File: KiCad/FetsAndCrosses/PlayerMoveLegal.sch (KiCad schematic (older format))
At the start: 0 parts

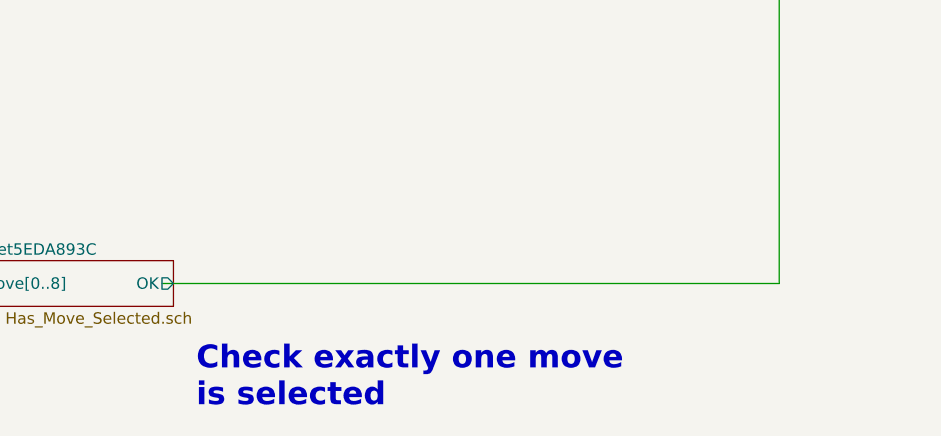
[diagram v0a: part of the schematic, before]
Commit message: Schematic Done, Footprints assigned, ERC OK.
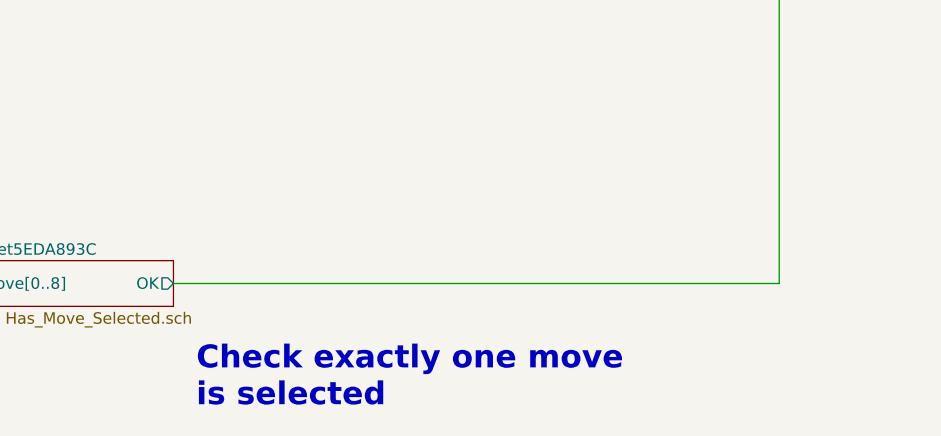
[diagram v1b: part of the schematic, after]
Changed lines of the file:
@@
 $Descr A4 11693 8268
 encoding utf-8
-Sheet 234 205
+Sheet 193 389
 Title ""
 Date ""
@@
 F4 "Move[0..8]" I L 4350 850 50
 $EndSheet
-Text Notes 5350 1500 0    100  ~ 20
-Check Selected Move \ndoes not collide with P1
-Text Notes 5350 3850 0    100  ~ 20
-Check Selected Move \ndoes not collide with P2
-Text Notes 5350 5800 0    100  ~ 20
-Check exactly one move\nis selected
 $Sheet
 S 8500 650  550  400
@@
 F5 "Q" O R 9050 850 50
 $EndSheet
+$Sheet
+S 4350 5150 900  200
+U 5EDA893D
+F0 "Sheet5EDA893C" 50
+F1 "Has_Move_Selected.sch" 50
+F2 "OK" O R 5250 5250 50
+F3 "Move[0..8]" I L 4350 5250 50
+$EndSheet
+Text Notes 5350 1500 0    100  ~ 20
+Check Selected Move \ndoes not collide with P1
+Text Notes 5350 3850 0    100  ~ 20
+Check Selected Move \ndoes not collide with P2
+Text Notes 5350 5800 0    100  ~ 20
+Check exactly one move\nis selected
 Text Notes 8700 900  0    100  ~ 20
 &
+Text HLabel 9450 850  2    50   Output ~ 0
+OK
+Text HLabel 1950 750  0    50   Input ~ 0
+Board_P1_[0..8]
+Text HLabel 2100 3000 0    50   Input ~ 0
+Board_P2_[0..8]
+Text HLabel 3700 5250 0    50   Input ~ 0
+Move[0..8]
+Text Label 3200 750  2    50   ~ 0
+Board_P1_[0..8]
+Text Label 3250 3000 2    50   ~ 0
+Board_P2_[0..8]
+Text Label 3500 750  0    50   ~ 0
+Board[0..8]
+Text Label 3550 3000 0    50   ~ 0
+Board[0..8]
 Wire Wire Line
 	5200 750  8500 750
@@
 	7800 3000 5200 3000
 Wire Wire Line
-	5200 5250 7900 5250
-Wire Wire Line
 	7900 5250 7900 950
 Wire Wire Line
@@
 Wire Wire Line
 	9050 850  9450 850
-Text HLabel 9450 850  2    50   Output ~ 0
-OK
-Text HLabel 1950 750  0    50   Input ~ 0
-Board_P1_[0..8]
-Text HLabel 2100 3000 0    50   Input ~ 0
-Board_P2_[0..8]
-Text HLabel 3700 5250 0    50   Input ~ 0
-Move[0..8]
-$Sheet
-S 4350 5150 900  200
-U 5EDA893D
-F0 "Sheet5EDA893C" 50
-F1 "Has_Move_Selected.sch" 50
-F2 "OK" O R 5250 5250 50
-F3 "Move[0..8]" I L 4350 5250 50
-$EndSheet
 Wire Bus Line
 	3700 5250 4150 5250
@@
 Wire Bus Line
 	4150 850  4350 850
-Connection ~ 4150 5250
 Wire Bus Line
 	4150 5250 4350 5250
 Wire Bus Line
 	4350 3100 4150 3100
-Connection ~ 4150 3100
 Wire Bus Line
 	4150 3100 4150 850
-Text Label 3200 750  2    50   ~ 0
-Board_P1_[0..8]
-Text Label 3250 3000 2    50   ~ 0
-Board_P2_[0..8]
-Text Label 3500 750  0    50   ~ 0
-Board[0..8]
-Text Label 3550 3000 0    50   ~ 0
-Board[0..8]
 Wire Bus Line
 	2100 3000 4350 3000
 Wire Bus Line
 	1950 750  4350 750
+Wire Wire Line
+	5250 5250 7900 5250
+Connection ~ 4150 5250
+Connection ~ 4150 3100
 $EndSCHEMATC

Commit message: Schematic fixes.
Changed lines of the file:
@@
 Sheet 193 389
 Title ""
-Date ""
-Rev ""
-Comp ""
-Comment1 ""
+Date "2020-07-05"
+Rev "v0.0"
+Comp "Philipp Schilk"
+Comment1 "c"
 Comment2 ""
 Comment3 ""
@@
 Text Label 3250 3000 2    50   ~ 0
 Board_P2_[0..8]
-Text Label 3500 750  0    50   ~ 0
-Board[0..8]
-Text Label 3550 3000 0    50   ~ 0
-Board[0..8]
 Wire Wire Line
 	5200 750  8500 750
